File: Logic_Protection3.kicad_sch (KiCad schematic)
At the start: 18 parts

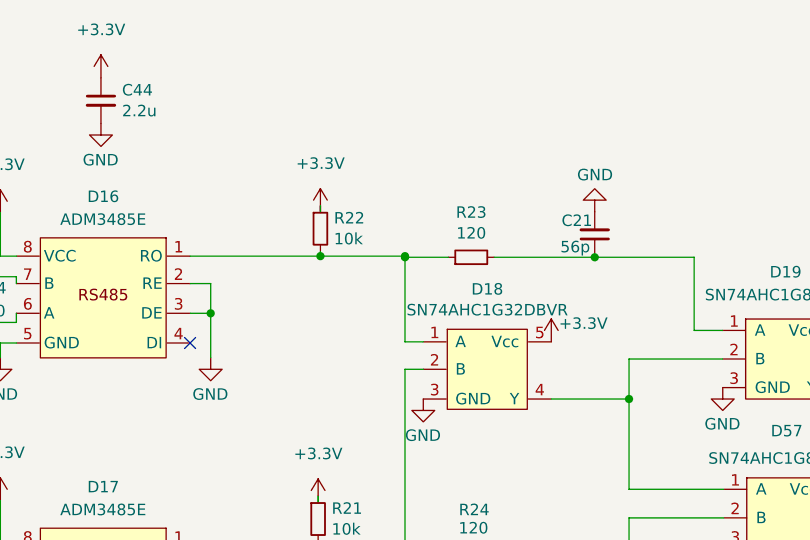
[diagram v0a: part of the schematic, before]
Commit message: Поменял компаратор на пушпульный
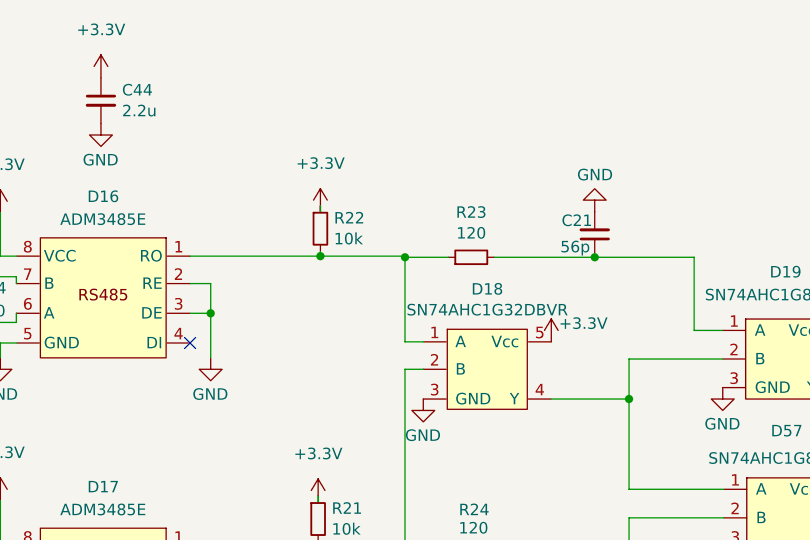
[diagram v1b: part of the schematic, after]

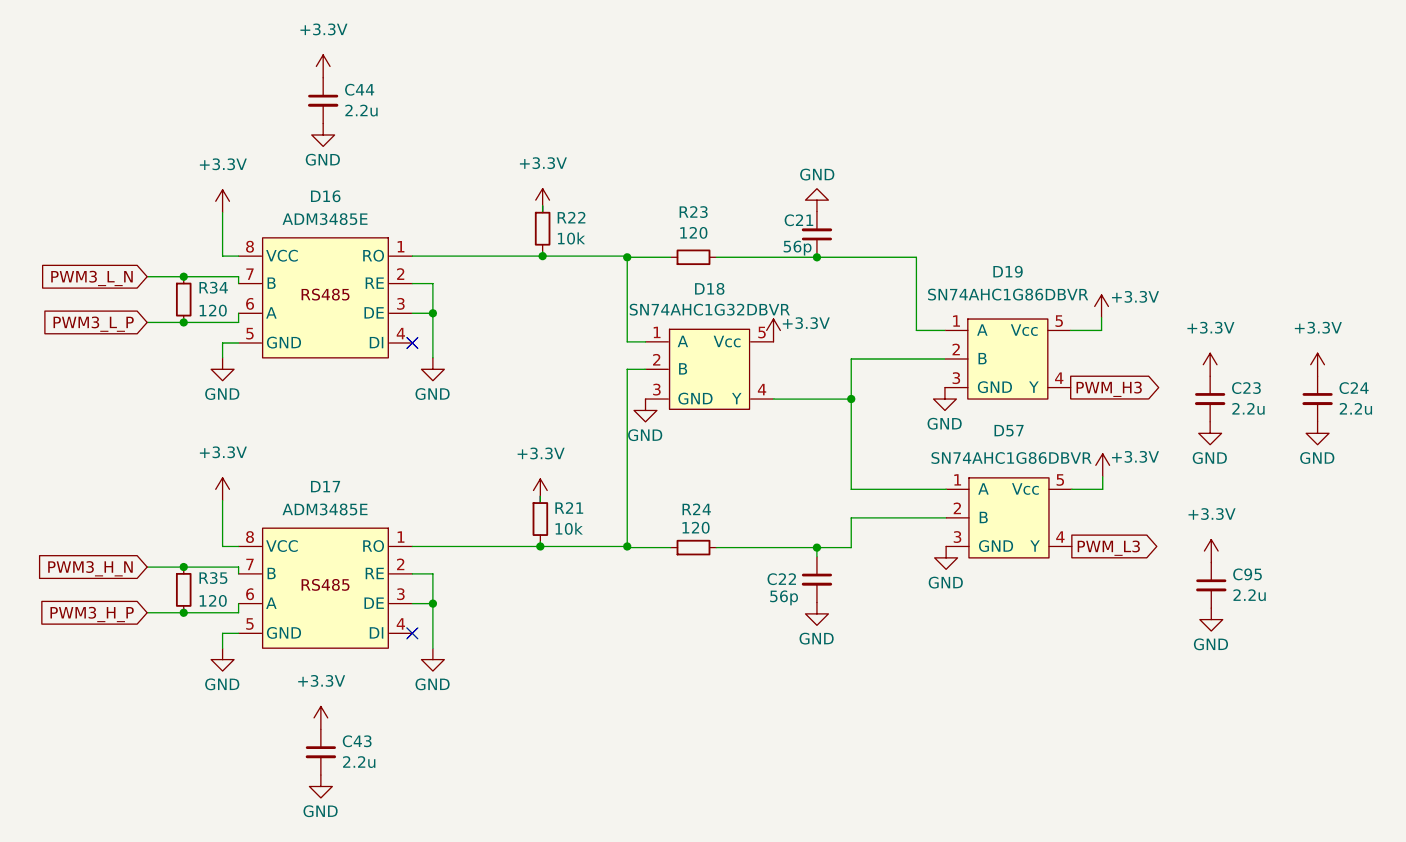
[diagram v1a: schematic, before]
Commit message: Изменил схему
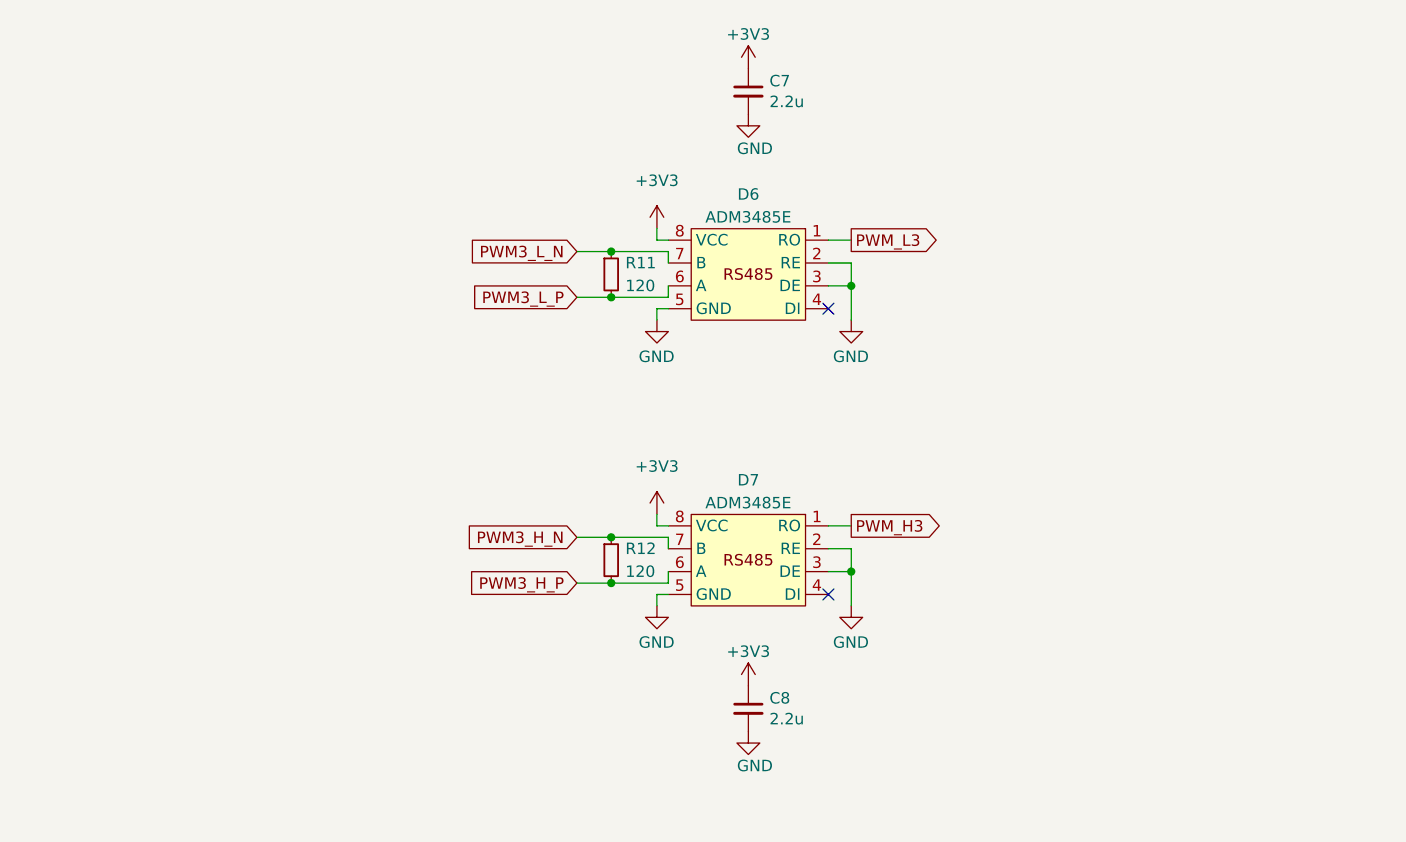
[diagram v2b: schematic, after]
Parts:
- removed C21, C22: 56p, Capacitor_SMD:C_0805_2012Metric_Pad1.18x1.45mm_HandSolder, symbol Device:C_Small
- removed C23, C24, C43, C44, C95: 2.2u, Capacitor_SMD:C_0805_2012Metric_Pad1.18x1.45mm_HandSolder, symbol Device:C_Small
- removed D16, D17: ADM3485E, Package_SO:SOIC-8_3.9x4.9mm_P1.27mm, symbol Interface_My:ADM3485E
- removed D18: SN74AHC1G32DBVR, Package_TO_SOT_SMD:SOT-23-5_HandSoldering, symbol Logic:SN74AHC1G86DBVR
- removed D19, D57: SN74AHC1G86DBVR, Package_TO_SOT_SMD:SOT-23-5_HandSoldering, symbol Logic:SN74AHC1G86DBVR
- removed R21, R22: 10k, Resistor_SMD:R_0805_2012Metric_Pad1.20x1.40mm_HandSolder, symbol Device:R_Small
- removed R23, R24, R34, R35: 120, Resistor_SMD:R_0805_2012Metric_Pad1.20x1.40mm_HandSolder, symbol Device:R_Small
- added C7, C8: 2.2u, Capacitor_SMD:C_0805_2012Metric_Pad1.18x1.45mm_HandSolder, symbol Device:C_Small
- added D6, D7: ADM3485E, Package_SO:SOIC-8_3.9x4.9mm_P1.27mm, symbol Interface_My:ADM3485E_1
- added R11, R12: 120, Resistor_SMD:R_0805_2012Metric_Pad1.20x1.40mm_HandSolder, symbol Device:R_Small
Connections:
- net +3V3: now also C7.1, C8.1, D6.8 (VCC), D7.8 (VCC)
- net GND: now also C7.2, C8.2, D6.2 (RE), D6.3 (DE), D6.5 (GND), D7.2 (RE), D7.3 (DE), D7.5 (GND)
- net PWM3_H_N: now also D7.7 (B), R12.1
- net PWM3_H_P: now also D7.6 (A), R12.2
- net PWM3_L_N: now also D6.7 (B), R11.1
- net PWM3_L_P: now also D6.6 (A), R11.2
- net PWM_H3: now also D7.1 (RO)
- net PWM_L3: now also D6.1 (RO)

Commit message: Убрал питание 3.3В
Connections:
- net +3V3 renamed +5V
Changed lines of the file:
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@@
 	)
 	(symbol
-		(lib_id "power:+3.3V")
+		(lib_id "power:+5V")
 		(at 140.97 113.03 0)
 		(unit 1)
@@
 		(dnp no)
 		(fields_autoplaced yes)
-		(property "Reference" "#PWR041"
+		(property "Reference" "#PWR41"
 			(at 140.97 116.84 0)
 			(effects
@@
 			)
 		)
-		(property "Value" "+3V3"
-			(at 140.97 107.696 0)
+		(property "Value" "+5V"
+			(at 140.97 107.95 0)
 			(effects
 				(font
@@
 			)
 		)
-		(property "Description" ""
+		(property "Description" "Power symbol creates a global label with name \"+5V\""
 			(at 140.97 113.03 0)
 			(effects
@@
 			(project "Adapter"
 				(path "/e63e39d7-6ac0-4ffd-8aa3-1841a4541b55/db5d7e63-27d7-4aee-825c-495c36afbd19"
-					(reference "#PWR041")
+					(reference "#PWR41")
 					(unit 1)
 				)
@@
 	)
 	(symbol
-		(lib_id "power:+3.3V")
+		(lib_id "power:+5V")
 		(at 151.13 132.08 0)
 		(unit 1)
@@
 		(on_board yes)
 		(dnp no)
-		(property "Reference" "#PWR046"
+		(property "Reference" "#PWR46"
 			(at 151.13 135.89 0)
 			(effects
@@
 			)
 		)
-		(property "Value" "+3V3"
-			(at 151.13 128.27 0)
+		(property "Value" "+5V"
+			(at 151.13 128.524 0)
 			(effects
 				(font
@@
 			)
 		)
-		(property "Description" ""
+		(property "Description" "Power symbol creates a global label with name \"+5V\""
 			(at 151.13 132.08 0)
 			(effects
@@
 			(project "Adapter"
 				(path "/e63e39d7-6ac0-4ffd-8aa3-1841a4541b55/db5d7e63-27d7-4aee-825c-495c36afbd19"
-					(reference "#PWR046")
+					(reference "#PWR46")
 					(unit 1)
 				)
@@
 	)
 	(symbol
-		(lib_id "power:+3.3V")
+		(lib_id "power:+5V")
 		(at 151.13 63.5 0)
 		(unit 1)
@@
 		(on_board yes)
 		(dnp no)
-		(property "Reference" "#PWR036"
+		(property "Reference" "#PWR36"
 			(at 151.13 67.31 0)
 			(effects
@@
 			)
 		)
-		(property "Value" "+3V3"
-			(at 151.13 59.69 0)
+		(property "Value" "+5V"
+			(at 151.13 59.944 0)
 			(effects
 				(font
@@
 			)
 		)
-		(property "Description" ""
+		(property "Description" "Power symbol creates a global label with name \"+5V\""
 			(at 151.13 63.5 0)
 			(effects
@@
 			(project "Adapter"
 				(path "/e63e39d7-6ac0-4ffd-8aa3-1841a4541b55/db5d7e63-27d7-4aee-825c-495c36afbd19"
-					(reference "#PWR036")
+					(reference "#PWR36")
 					(unit 1)
 				)
@@
 	)
 	(symbol
-		(lib_id "power:+3.3V")
+		(lib_id "power:+5V")
 		(at 140.97 81.28 0)
 		(unit 1)
@@
 		(dnp no)
 		(fields_autoplaced yes)
-		(property "Reference" "#PWR038"
+		(property "Reference" "#PWR38"
 			(at 140.97 85.09 0)
 			(effects
@@
 			)
 		)
-		(property "Value" "+3V3"
-			(at 140.97 75.946 0)
+		(property "Value" "+5V"
+			(at 140.97 76.2 0)
 			(effects
 				(font
@@
 			)
 		)
-		(property "Description" ""
+		(property "Description" "Power symbol creates a global label with name \"+5V\""
 			(at 140.97 81.28 0)
 			(effects
@@
 			(project "Adapter"
 				(path "/e63e39d7-6ac0-4ffd-8aa3-1841a4541b55/db5d7e63-27d7-4aee-825c-495c36afbd19"
-					(reference "#PWR038")
-					(unit 1)
-				)
+					(reference "#PWR38")
+					(unit 1)
+				)

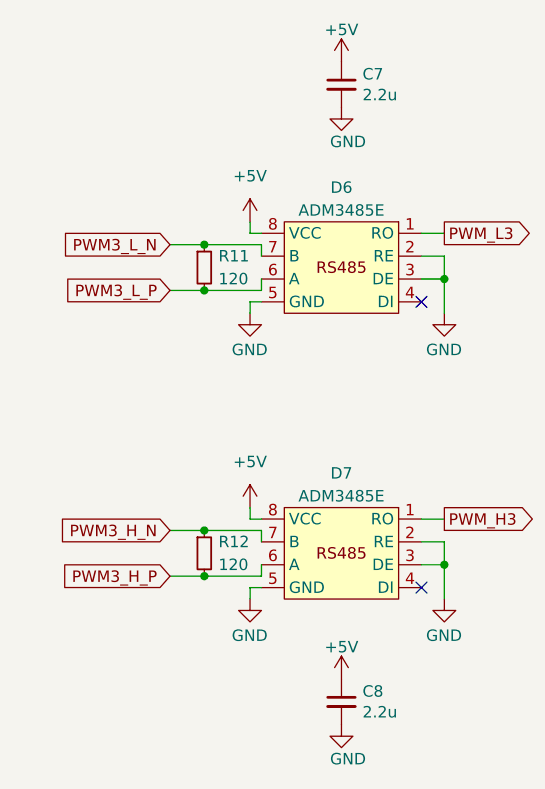
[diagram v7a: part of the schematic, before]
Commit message: Изменения: добавил подтяжки шины RS485
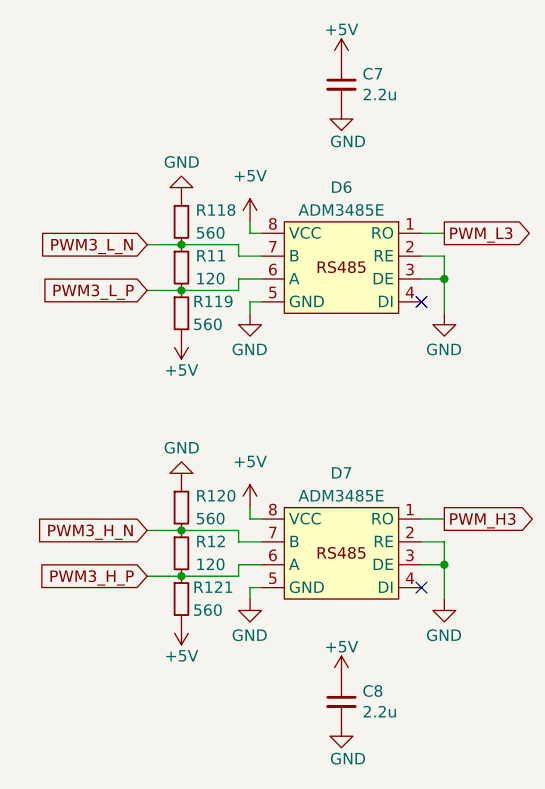
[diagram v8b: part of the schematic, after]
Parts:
- added R118, R119, R120, R121: 560, Resistor_SMD:R_0805_2012Metric_Pad1.20x1.40mm_HandSolder, symbol Device:R_Small
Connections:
- net +5V: now also R119.2, R121.2
- net GND: now also R118.1, R120.1
- net PWM3_H_N: now also R120.2
- net PWM3_H_P: now also R121.1
- net PWM3_L_N: now also R118.2
- net PWM3_L_P: now also R119.1
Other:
- moved on the sheet: R11, R12
